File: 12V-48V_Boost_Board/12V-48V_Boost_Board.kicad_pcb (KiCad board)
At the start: 2 copper layers, 65.1 x 76.7 mm, 42 parts, among them J1 12V Input, J2 Input Current Sensing, J3 Output Current Sensing, J4 48V Output, J5 Output Measuring, Q1 FDWS86068-F085, U2 INA290

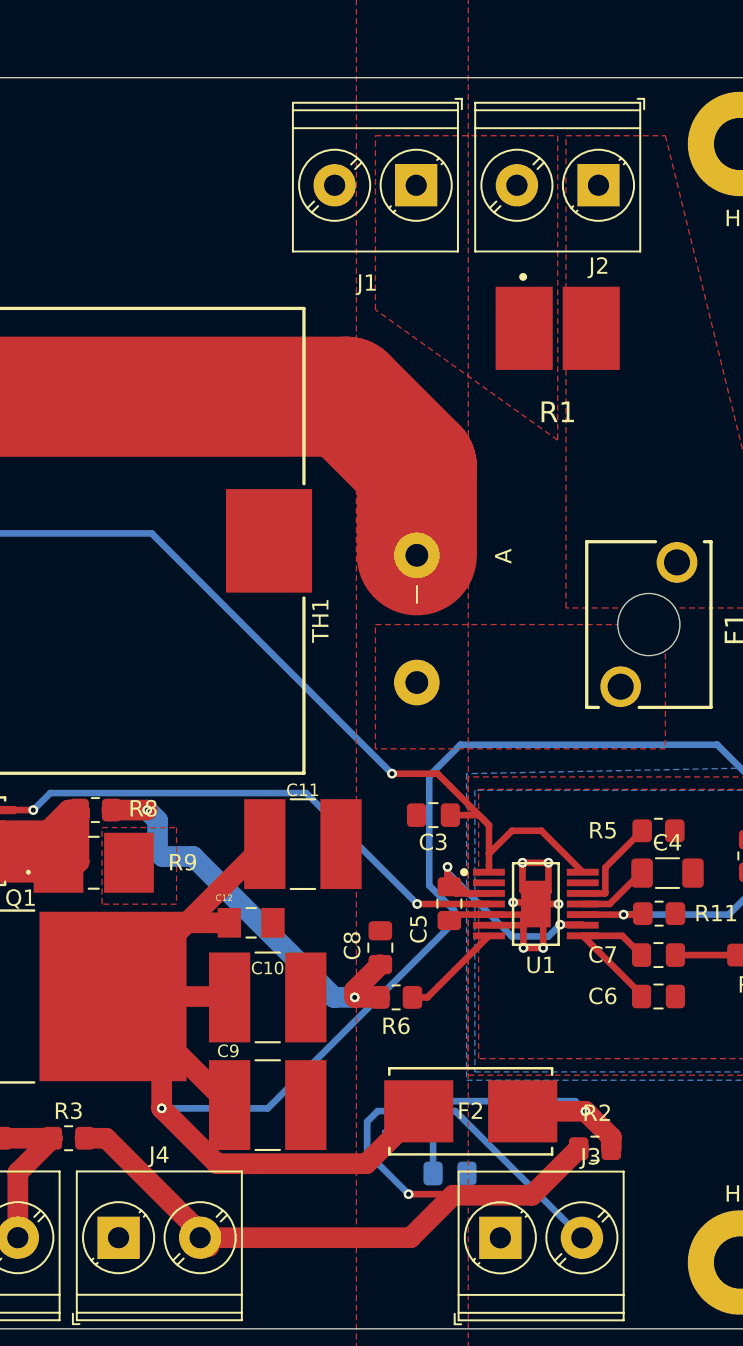
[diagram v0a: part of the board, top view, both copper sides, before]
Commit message: Added second op-amp, need to add 5 volt input
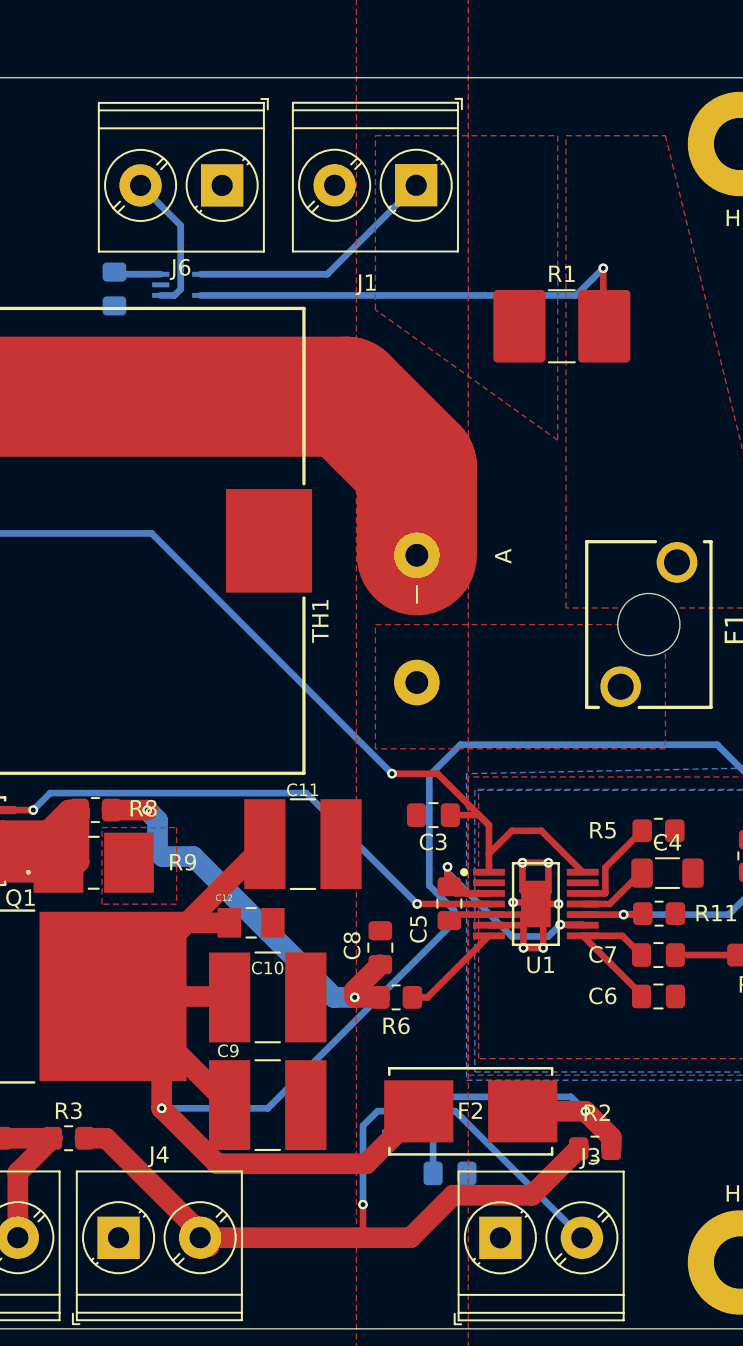
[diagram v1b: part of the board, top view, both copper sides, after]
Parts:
- removed J2: Input Current Sensing, TerminalBlock_Phoenix:TerminalBlock_Phoenix_PT-1,5-2-5.0-H_1x02_P5.00mm_Horizontal
- added C14: 0.1uF, Capacitor_SMD:C_0805_2012Metric_Pad1.18x1.45mm_HandSolder, B.Cu at (129.3, 81.0)
- added J6: Output Current Sensing, TerminalBlock_Phoenix:TerminalBlock_Phoenix_PT-1,5-2-5.0-H_1x02_P5.00mm_Horizontal, F.Cu at (135.9, 74.7)
- added U3: INA290, 12/48 boost:SC70-5_DCK_TEX, B.Cu at (133.3, 80.8)
- R1: value 1mΩ -> 5mΩ; footprint 12/48 boost:WSHM28181L000FEA -> Resistor_SMD:R_2816_7142Metric_Pad3.20x4.45mm_HandSolder
- moved R1 0.28 mm to (156.7, 83.3)
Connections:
- net Net-(J1-Pin_1) renamed /IN+
- net Net-(J2-Pin_1) renamed /IN-
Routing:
- net /IN-: track 0.00 -> 29.0 mm, vias 0 -> 1
- net /IN+: track 0.00 -> 15.5 mm
- net Net-(J6-Pin_2): track 0.00 -> 8.77 mm
- net +5V: track 2.59 -> 5.48 mm
- net Net-(J4-Pin_2): track 46.0 -> 45.0 mm

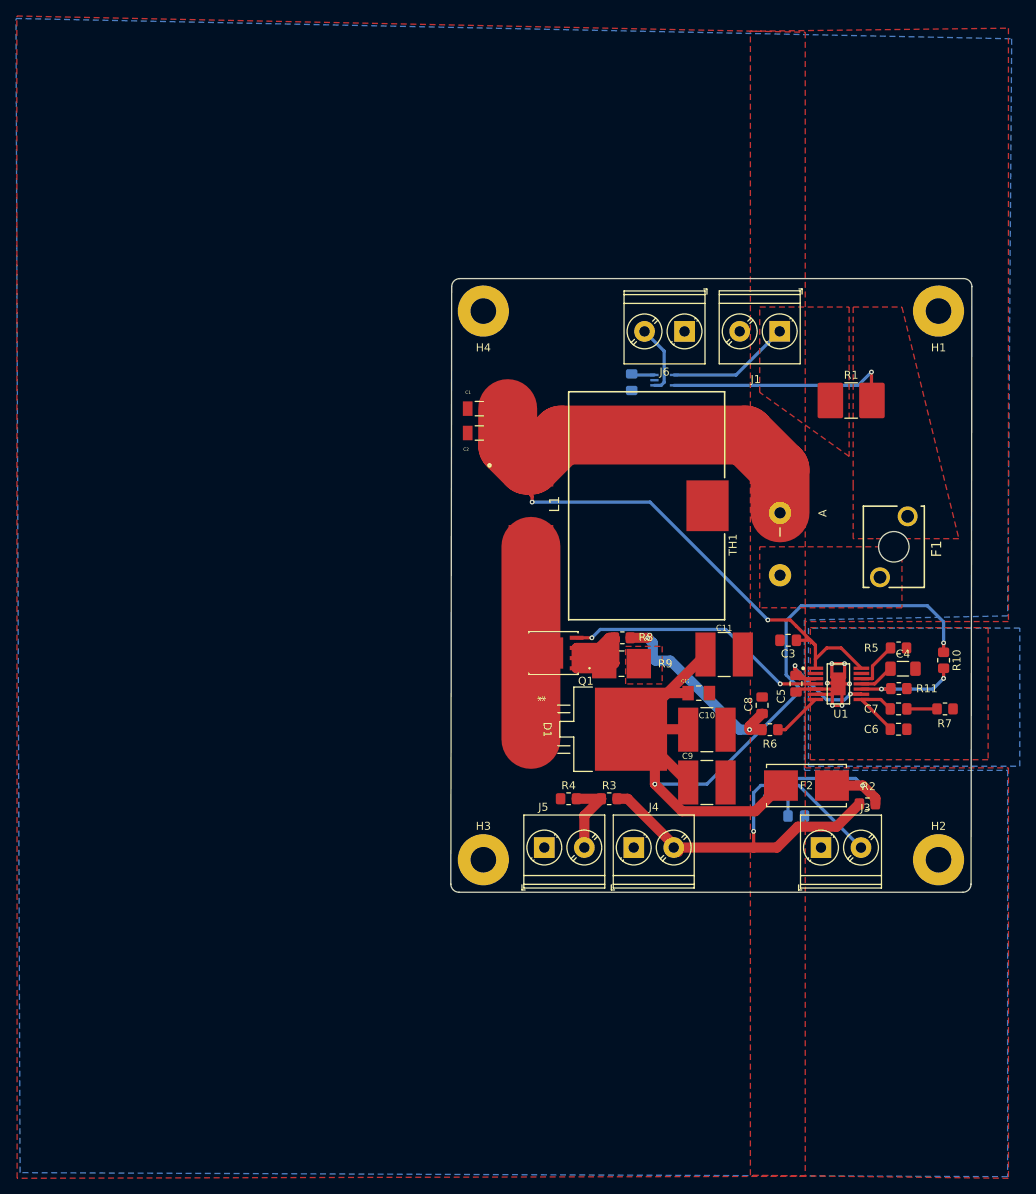
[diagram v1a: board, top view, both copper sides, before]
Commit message: Schematic and PCB changes. See descp.
- Added 12V to 5V LDO to schematic and PCB.
- Via stitched large planes both due to thermal and GND return path concerns.
- Other minor tweaks.
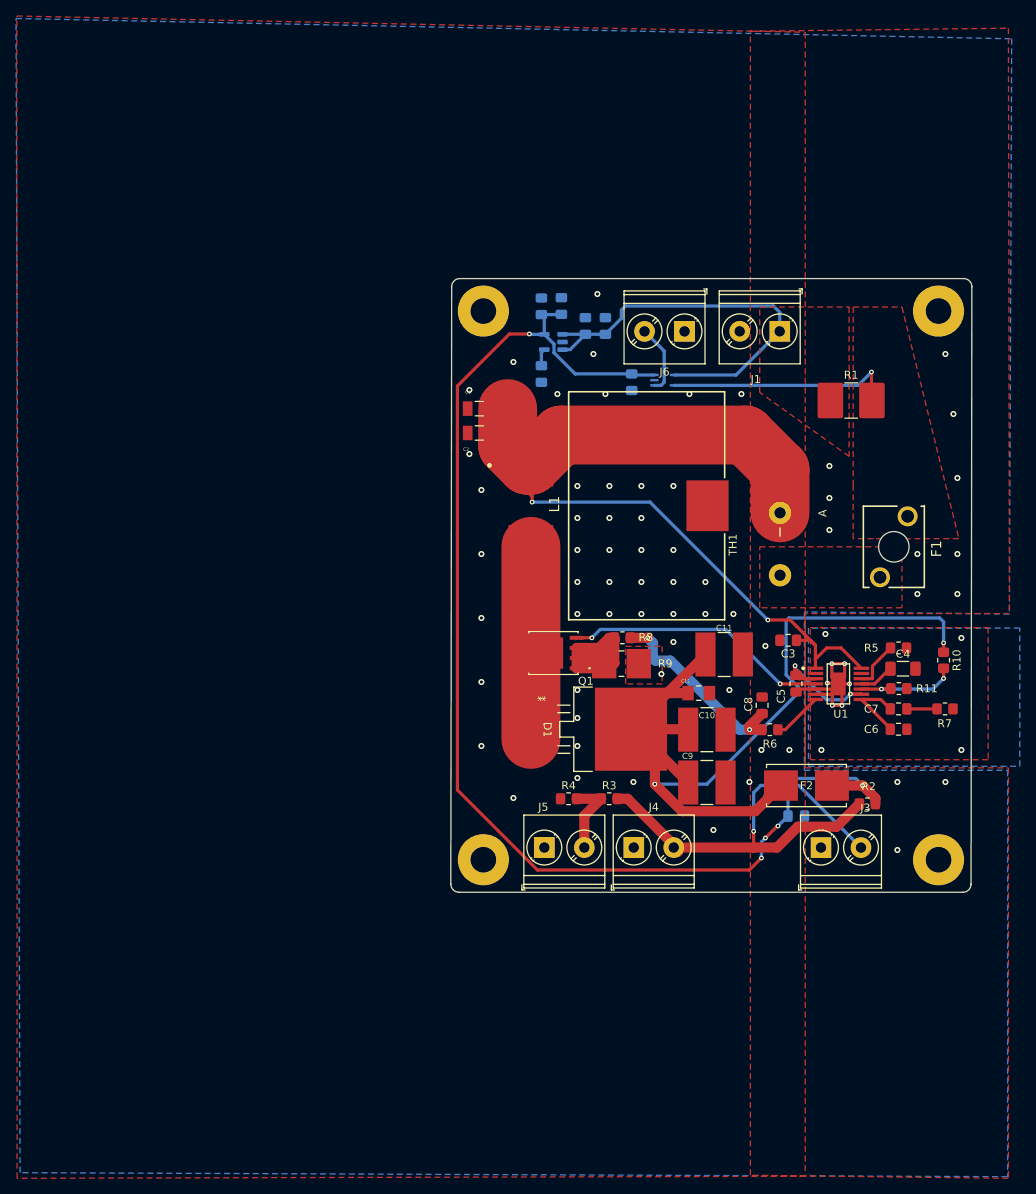
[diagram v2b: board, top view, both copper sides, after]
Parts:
- added C15: 100nF, Capacitor_SMD:C_0805_2012Metric_Pad1.18x1.45mm_HandSolder, B.Cu at (126.0, 74.0)
- added C16: 1uF, Capacitor_SMD:C_0805_2012Metric_Pad1.18x1.45mm_HandSolder, B.Cu at (123.5, 74.0)
- added C17: 100nF, Capacitor_SMD:C_0805_2012Metric_Pad1.18x1.45mm_HandSolder, B.Cu at (120.5, 71.5)
- added C20: 2.2uF, Capacitor_SMD:C_0805_2012Metric_Pad1.18x1.45mm_HandSolder, B.Cu at (118.0, 71.5)
- added C21: 10nF, Capacitor_SMD:C_0805_2012Metric_Pad1.18x1.45mm_HandSolder, B.Cu at (118.0, 80.0)
- added U4: LP2985-5.0, Package_TO_SOT_SMD:SOT-23-5, B.Cu at (119.5, 76.0)
- U2, U3: value INA290 -> INA290A3
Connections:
- net /IN+ renamed +12V
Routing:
- net +5V: track 5.48 -> 137.7 mm, vias 0 -> 4
- net +12V: track 15.5 -> 51.1 mm
- net Net-(U4-BP): track 0.00 -> 2.16 mm
- net /Boost_Board_Chip/48V_OUTPUT: track 123.9 -> 122.6 mm
- net GND: vias 6 -> 73

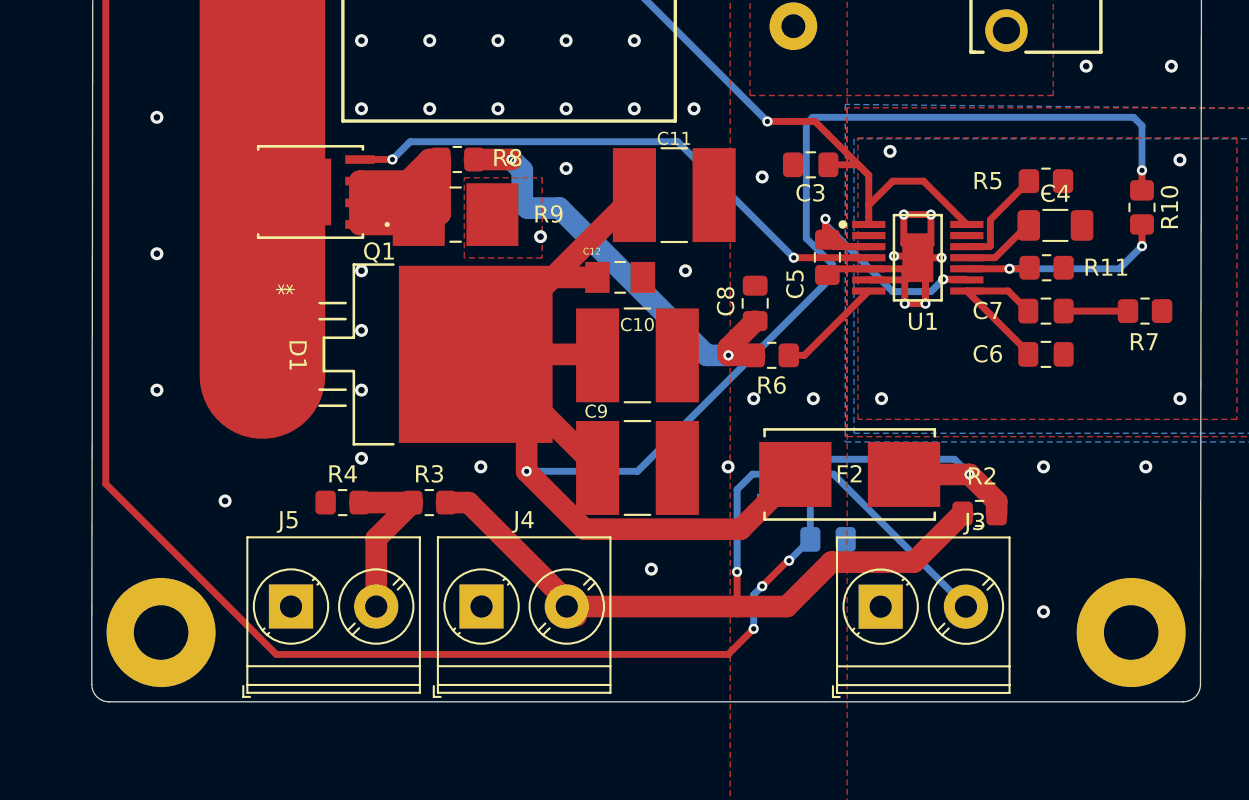
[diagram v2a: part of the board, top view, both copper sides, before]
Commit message: Updated routing and component placement to optimize ground return.
Next: move input 5V LDO and omp amp to top layer in order not to obstruct gnd path.
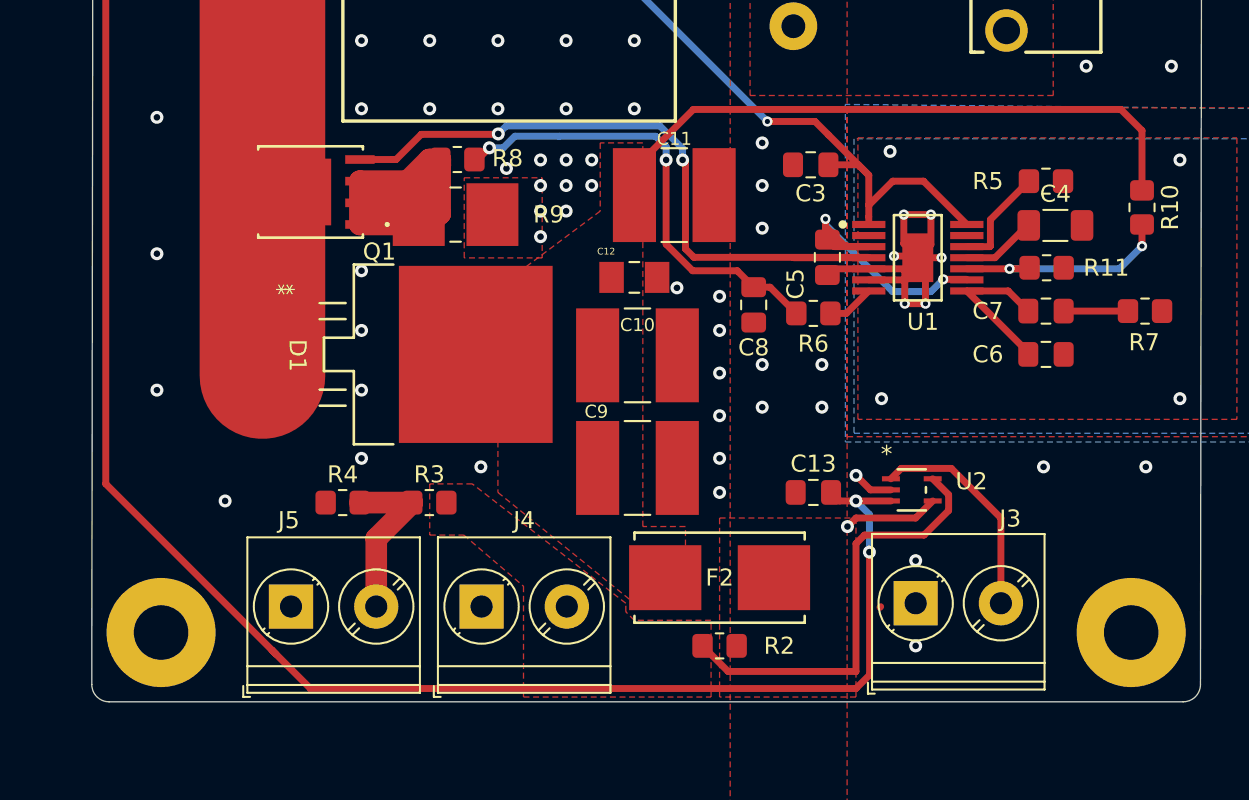
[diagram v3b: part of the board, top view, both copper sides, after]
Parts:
- C13, U2: moved to F.Cu
- moved R2 17.1 mm to (143.5, 141.5)
- moved F2 9.74 mm to (143.5, 137.5)
- moved U2 7.33 mm to (154.8, 132.4), turned to 0 degrees
- moved R6 3.47 mm to (149.0, 122.0)
- moved C13 2.89 mm to (149.0, 132.5), turned to 0 degrees
- moved J3 2.06 mm to (155.0, 139.0)
- moved C12 0.83 mm to (138.5, 119.9)
- moved C8 0.12 mm to (145.5, 121.5), turned to -90 degrees
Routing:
- net /Boost_Board_Chip/48V_OUTPUT: track 122.6 -> 42.2 mm, vias 2 -> 0
- net Net-(J4-Pin_2): track 45.0 -> 25.9 mm, vias 1 -> 0
- net Net-(U2-IN+): track 20.2 -> 5.62 mm
- net +5V: track 137.7 -> 150.4 mm, vias 4 -> 3
- net Net-(Q1-G): track 33.1 -> 41.6 mm
- net Net-(U1-CS): track 6.26 -> 2.80 mm
- net GND: track 23.8 -> 26.2 mm, vias 73 -> 90
- net Net-(C8-Pad1): track 25.0 -> 27.1 mm
- added copper zone on F.Cu, net /Boost_Board_Chip/48V_OUTPUT
- added copper zone on F.Cu, net Net-(J4-Pin_2)
- added copper zone on F.Cu, net Net-(U2-IN+)
